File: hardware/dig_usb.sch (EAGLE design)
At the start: 123 parts, among them IC201 ATMEGA32A-AU, IC202 DS1337S, IC203 MAX487CSA, IC204 74HC166D, IC205 74HC595D, IC301 LTV-356T, IC302 LTV-356T, IC303 LTV-356T, IC304 LTV-356T, IC305 LTV-356T, IC306 LTV-356T, IC307 LTV-356T, IC308 LTV-356T, K401 S202S02, K402 S202S02, K403 S202S02, K404 S202S02, K405 S202S02, K406 S202S02, K407 S202S02, K408 S202S02, Q201 32,768kHz, T301 BCR191, T302 BCR191, T303 BCR191, T304 BCR191, T305 BCR191, T306 BCR191, T307 BCR191, T308 BCR191, X101 RIA-73-02, X201 ISP, X202 RIA-73-02, X301 RIA-73-02, X302 RIA-73-02, X303 RIA-73-02, X304 RIA-73-02, X305 RIA-73-02, X401 RIA-73-02, X402 RIA-73-02, X403 RIA-73-02, X404 RIA-73-02, X405 RIA-73-02

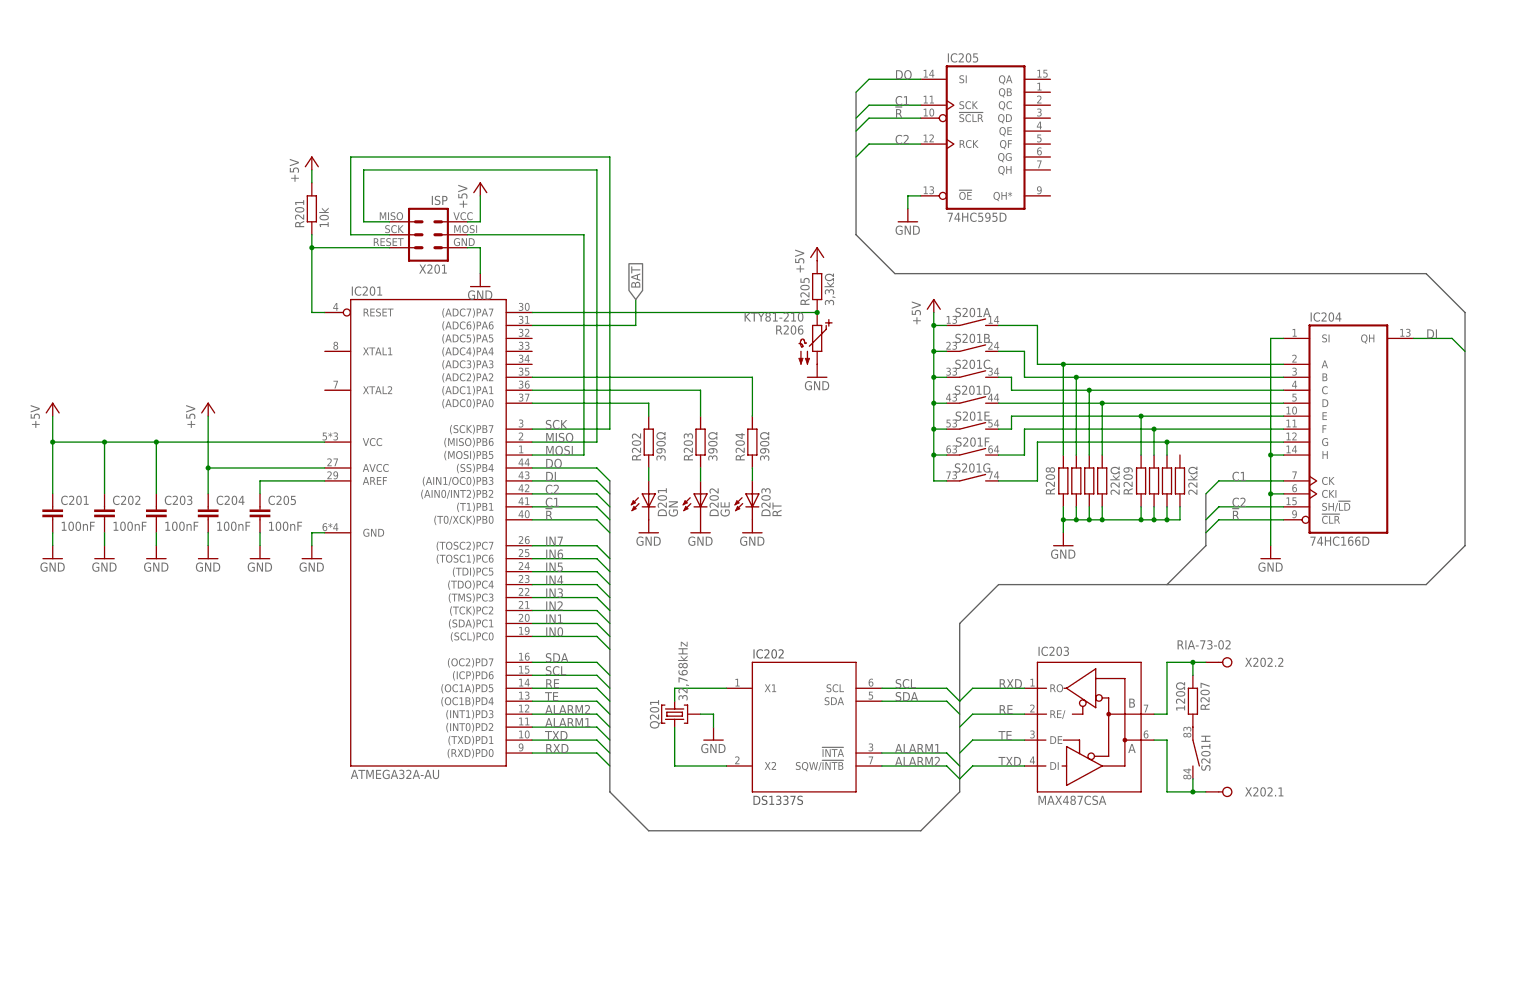
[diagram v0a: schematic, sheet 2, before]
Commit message: dig_usb auf AT90USB1287 umgestellt
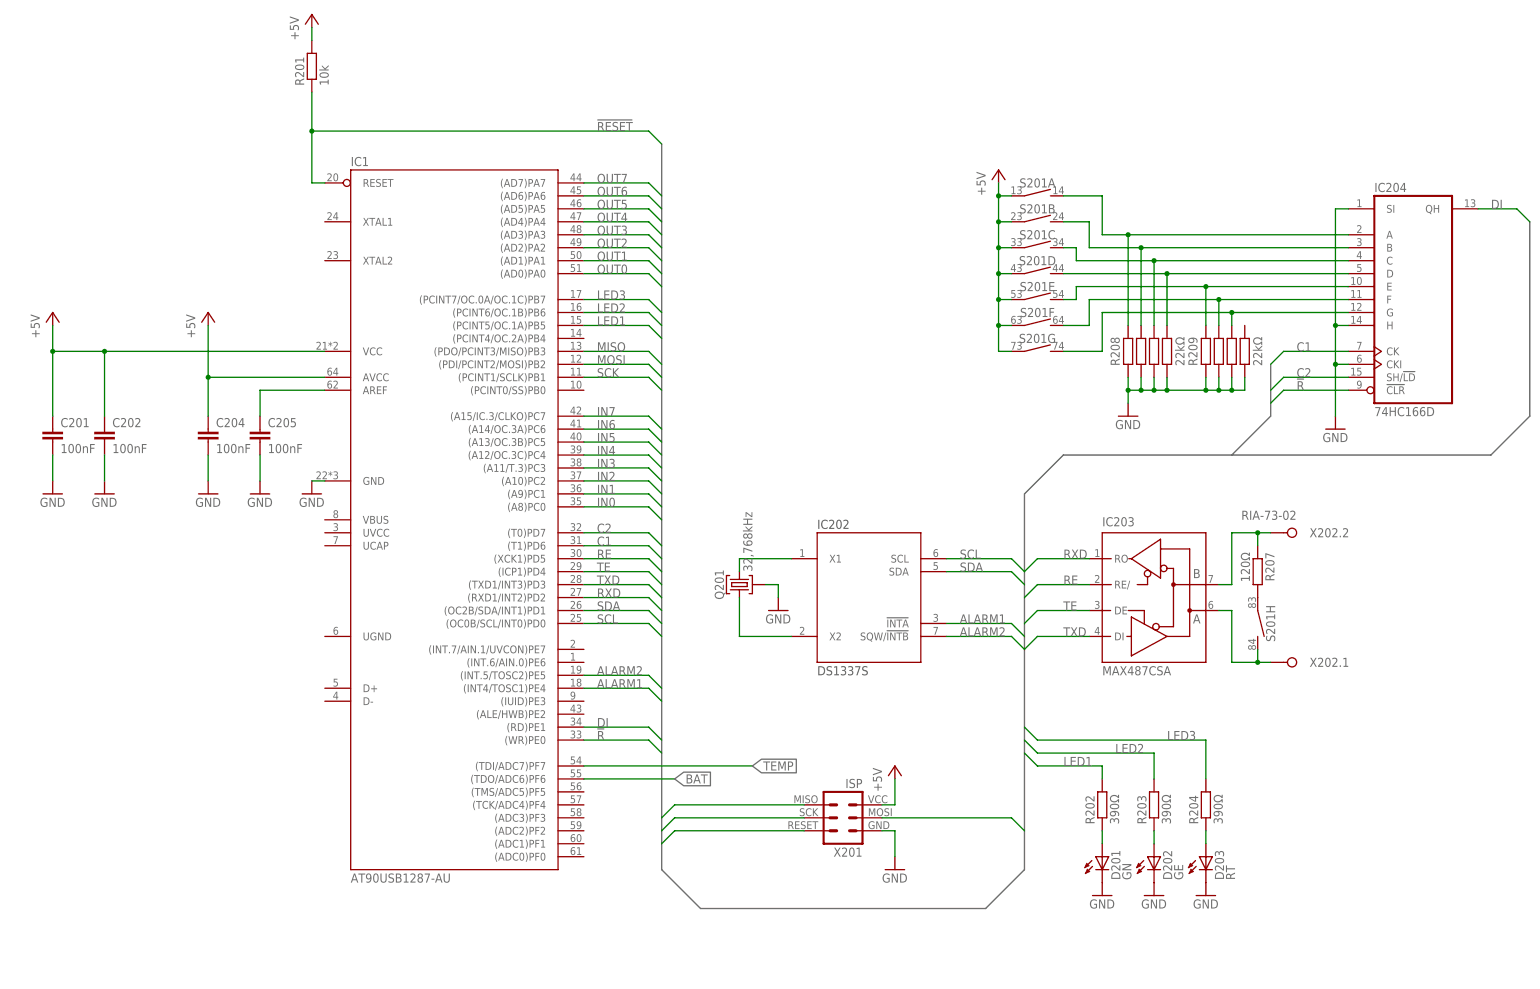
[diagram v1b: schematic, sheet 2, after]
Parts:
- removed C103, C203: 100nF, passiv:C_0603
- removed IC201: ATMEGA32A-AU, ic-mcu:ATMEGA32A-AU
- removed IC205: 74HC595D, ic-logik:74HC595D
- added IC1: AT90USB1287-AU, ic-mcu:AT90USB1287-AU
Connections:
- removed net DO: IC201.(SS)PB4, IC205A.SI
- removed net N$25: C205.1, IC201.AREF
- removed net N$42: IC201.RESET, R201.1, X201.RESET
- removed net N$61: IC201.(ADC7)PA7, R205.1, R206.1
- removed net N$8: IC201.(ADC2)PA2, R204.2
- removed net N$90: IC201.(ADC0)PA0, R202.2
- removed net N$92: IC201.(ADC1)PA1, R203.2
- new net !RESET: IC1.RESET, R201.1, X201.RESET
- new net LED1: IC1.(PCINT5/OC.1A)PB5, R202.2
- new net LED2: IC1.(PCINT6/OC.1B)PB6, R203.2
- new net LED3: IC1.(PCINT7/OC.0A/OC.1C)PB7, R204.2
- new net N$12: C205.1, IC1.AREF
- new net OUT0: IC1.(AD0)PA0
- new net OUT1: IC1.(AD1)PA1
- new net OUT2: IC1.(AD2)PA2
- new net OUT3: IC1.(AD3)PA3
- new net OUT4: IC1.(AD4)PA4
- new net OUT5: IC1.(AD5)PA5
- new net OUT6: IC1.(AD6)PA6
- new net OUT7: IC1.(AD7)PA7
- new net TEMP: IC1.(TDI/ADC7)PF7, R205.1, R206.1
- net !R: now also IC1.(WR)PE0; no longer IC201.(T0/XCK)PB0, IC205A.!SCLR
- net +5V: now also IC1.AVCC, IC1.VCC; no longer C103.1, C203.1, IC201.AVCC, IC201.VCC, IC205P.VCC
- net ALARM1: now also IC1.(INT4/TOSC1)PE4; no longer IC201.(INT0)PD2
- net ALARM2: now also IC1.(INT.5/TOSC2)PE5; no longer IC201.(INT1)PD3
- net BAT: now also IC1.(TDO/ADC6)PF6; no longer IC201.(ADC6)PA6
- net C1: now also IC1.(T1)PD6; no longer IC201.(T1)PB1, IC205A.SCK
- net C2: now also IC1.(T0)PD7; no longer IC201.(AIN0/INT2)PB2, IC205A.RCK
- net DI: now also IC1.(RD)PE1; no longer IC201.(AIN1/OC0)PB3
- net GND: now also IC1.GND; no longer C103.2, C203.2, IC201.GND, IC205A.!OE, IC205P.GND
- net IN0: now also IC1.(A8)PC0; no longer IC201.(SCL)PC0
- net IN1: now also IC1.(A9)PC1; no longer IC201.(SDA)PC1
- net IN2: now also IC1.(A10)PC2; no longer IC201.(TCK)PC2
- net IN3: now also IC1.(A11/T.3)PC3; no longer IC201.(TMS)PC3
- net IN4: now also IC1.(A12/OC.3C)PC4; no longer IC201.(TDO)PC4
- net IN5: now also IC1.(A13/OC.3B)PC5; no longer IC201.(TDI)PC5
- net IN6: now also IC1.(A14/OC.3A)PC6; no longer IC201.(TOSC1)PC6
- net IN7: now also IC1.(A15/IC.3/CLKO)PC7; no longer IC201.(TOSC2)PC7
- net MISO: now also IC1.(PDO/PCINT3/MISO)PB3; no longer IC201.(MISO)PB6
- net MOSI: now also IC1.(PDI/PCINT2/MOSI)PB2; no longer IC201.(MOSI)PB5
- net RE: now also IC1.(XCK1)PD5; no longer IC201.(OC1A)PD5
- net RXD: now also IC1.(RXD1/INT2)PD2; no longer IC201.(RXD)PD0
- net SCK: now also IC1.(PCINT1/SCLK)PB1; no longer IC201.(SCK)PB7
- net SCL: now also IC1.(OC0B/SCL/INT0)PD0; no longer IC201.(ICP)PD6
- net SDA: now also IC1.(OC2B/SDA/INT1)PD1; no longer IC201.(OC2)PD7
- net TE: now also IC1.(ICP1)PD4; no longer IC201.(OC1B)PD4
- net TXD: now also IC1.(TXD1/INT3)PD3; no longer IC201.(TXD)PD1
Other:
- moved on the sheet: C104, C201, C202, C204, C205, D103, D104, D201, D202, D203, G102, IC202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

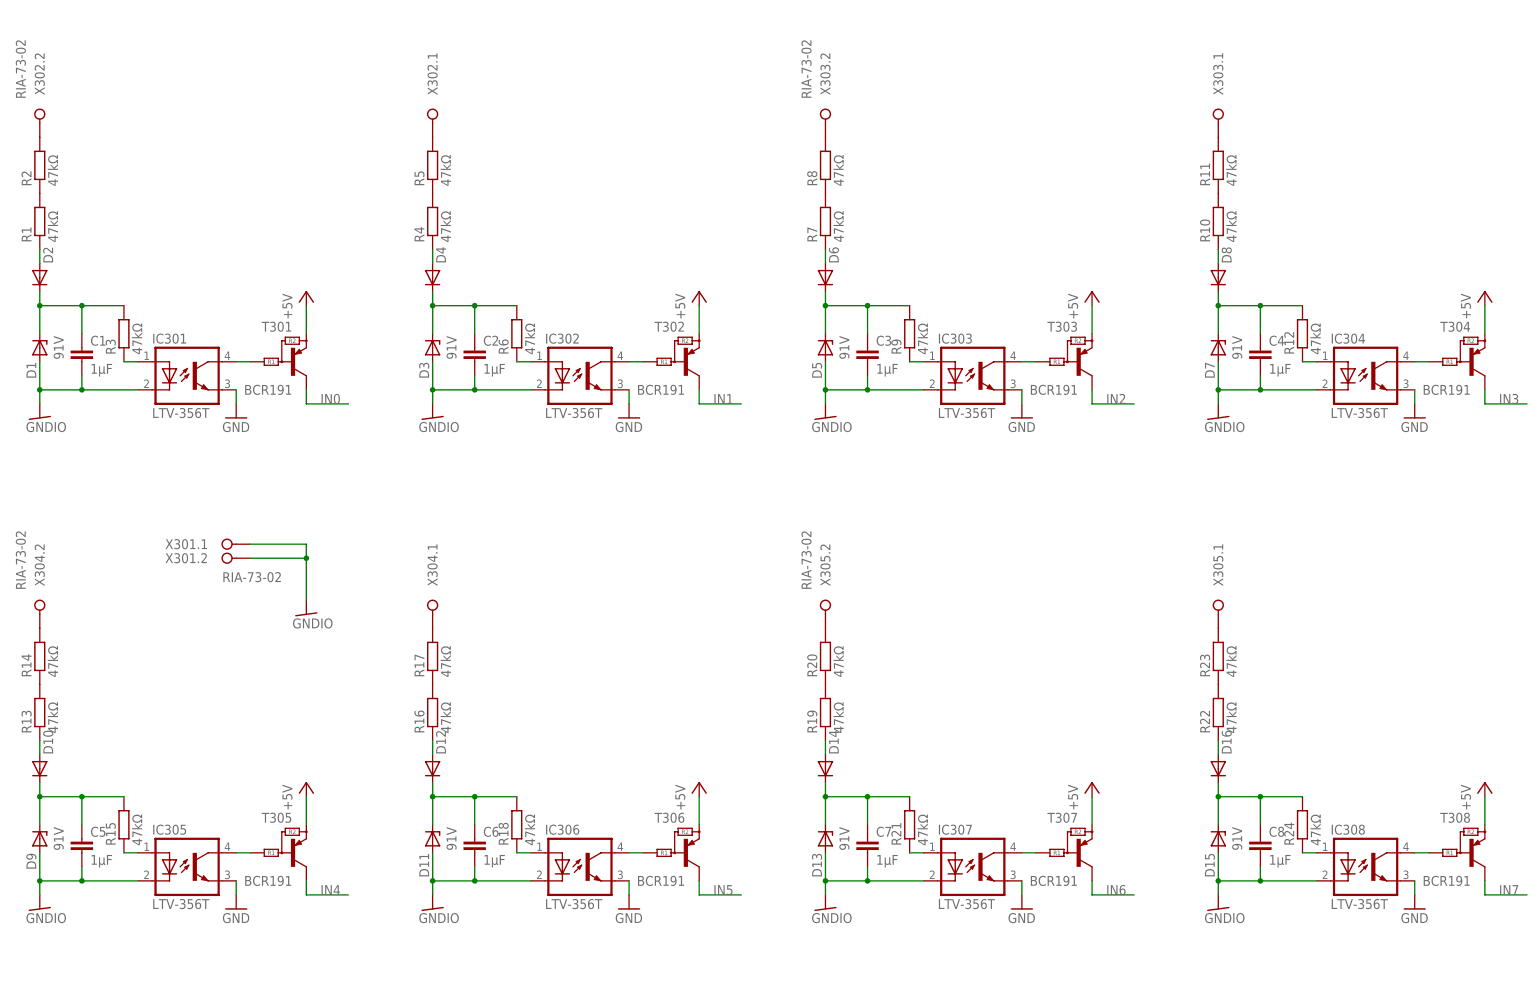
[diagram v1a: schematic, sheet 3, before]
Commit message: IO Bereich der unteren Platine geroutet
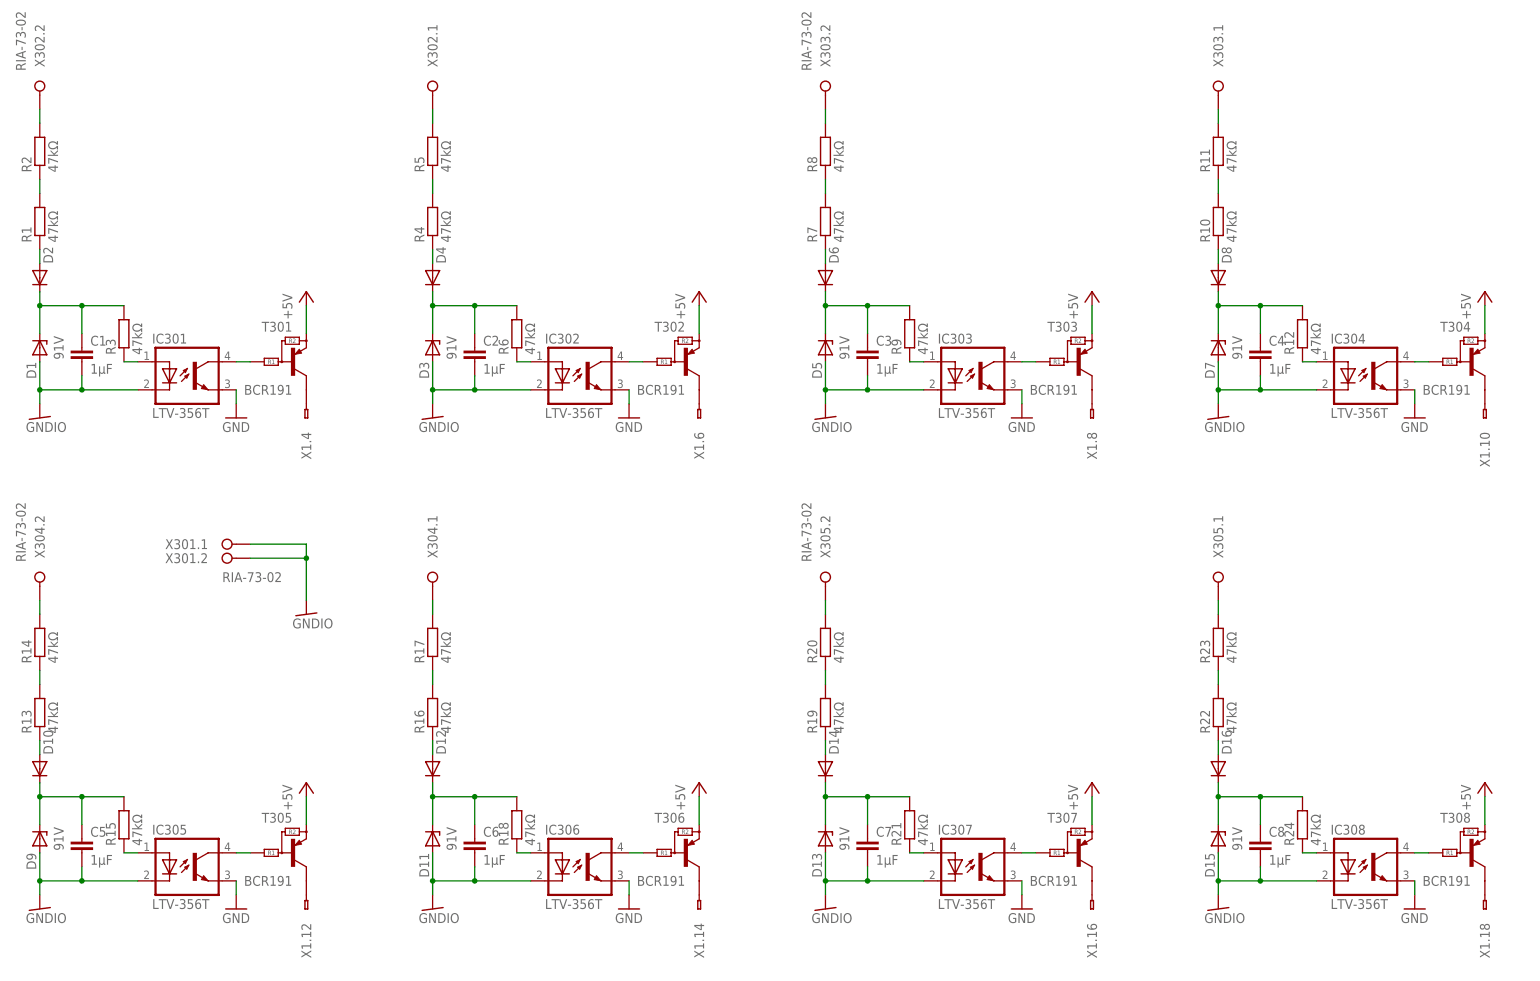
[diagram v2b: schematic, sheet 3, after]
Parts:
- removed R205: 3,3kΩ, passiv:R_0805
- removed R206: KTY81-210, sensor:KTY81-210
- added R401, R402, R403, R404, R405, R406, R407, R408: (no value), passiv:R_0805
- added R409: 3,3kΩ, passiv:R_0805
- added R410: KTY81-210, sensor:KTY81-210
- added X1: (no value), anschluss:WS20V
- G102: value KZH20P -> KZH20SMD-2; device batterie:KZH20P -> batterie:KZH20SMD-2
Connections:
- new net N$100: T307.C, X1.16.A
- new net N$101: T308.C, X1.18.A
- new net N$16: K402.A, R402.2
- new net N$25: K403.A, R403.2
- new net N$37: K404.A, R404.2
- new net N$42: K405.A, R405.2
- new net N$50: K406.A, R406.2
- new net N$61: K407.A, R407.2
- new net N$66: K408.A, R408.2
- new net N$67: R401.1, X1.3.A
- new net N$79: R402.1, X1.5.A
- new net N$8: K401.A, R401.2
- new net N$87: R403.1, X1.7.A
- new net N$88: R404.1, X1.9.A
- new net N$90: R405.1, X1.11.A
- new net N$91: R406.1, X1.13.A
- new net N$92: R407.1, X1.15.A
- new net N$93: R408.1, X1.17.A
- new net N$94: T301.C, X1.4.A
- new net N$95: T302.C, X1.6.A
- new net N$96: T303.C, X1.8.A
- new net N$97: T304.C, X1.10.A
- new net N$98: T305.C, X1.12.A
- new net N$99: T306.C, X1.14.A
- net +5V: now also R409.2, X1.1.A, X1.20.A; no longer R205.2
- net GND: now also R410.2, X1.19.A, X1.2.A; no longer R206.2
- net IN0: no longer T301.C
- net IN1: no longer T302.C
- net IN2: no longer T303.C
- net IN3: no longer T304.C
- net IN4: no longer T305.C
- net IN5: no longer T306.C
- net IN6: no longer T307.C
- net IN7: no longer T308.C
- net TEMP: now also R409.1, R410.1; no longer R205.1, R206.1
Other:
- moved on the sheet: R11, R14, R17, R2, R20, R23, R5, R8, X302.1, X302.2, X303.1, X303.2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

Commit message: Einiges auf dig_usb controllerboard gerouted
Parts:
- removed R101, R202, R203, R204: 390Ω, passiv:R_0805
- added D17, D18, D19, D20, D21, D22, D23, D24, D25, D26, D27, D28, D29, D30, D31, D32: GN, led:LED_0805
- added R25, R26, R27, R28, R29: 1,5kΩ, widerstandsnetzwerk:EXB-38V
- added X2: (no value), anschluss:WS20V
- R401, R402, R403, R404, R405, R406, R407, R408: value (none) -> 470Ω
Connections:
- new net N$102: D17.A, R25.2
- new net N$103: D18.A, R25.4
- new net N$104: D19.A, R25.6
- new net N$105: D20.A, R25.8
- new net N$106: D21.A, R26.2
- new net N$107: D22.A, R26.4
- new net N$108: D23.A, R26.6
- new net N$109: D24.A, R26.8
- new net N$110: D25.A, R27.1
- new net N$111: D26.A, R27.3
- new net N$112: D27.A, R27.5
- new net N$113: D28.A, R27.7
- new net N$114: D29.A, R28.1
- new net N$115: D30.A, R28.3
- new net N$116: D31.A, R28.5
- new net N$117: D32.A, R28.7
- net +5V: now also R29.8, X2.1.A, X2.20.A; no longer R101.2
- net GND: now also D17.C, D18.C, D19.C, D20.C, D21.C, D22.C, D23.C, D24.C, D25.C, D26.C, D27.C, D28.C, D29.C, D30.C, D31.C, D32.C, X2.19.A, X2.2.A
- net IN0: now also R25.1, X2.4.A
- net IN1: now also R25.3, X2.6.A
- net IN2: now also R25.5, X2.8.A
- net IN3: now also R25.7, X2.10.A
- net IN4: now also R26.1, X2.12.A
- net IN5: now also R26.3, X2.14.A
- net IN6: now also R26.5, X2.16.A
- net IN7: now also R26.7, X2.18.A
- net LED1: now also R29.2; no longer R202.2
- net LED2: now also R29.4; no longer R203.2
- net LED3: now also R29.6; no longer R204.2
- net N$4: now also R29.5; no longer R204.1
- net N$44: now also R29.7; no longer R101.1
- net N$62: now also R29.1; no longer R202.1
- net N$63: now also R29.3; no longer R203.1
- net OUT0: now also R27.2, X2.3.A
- net OUT1: now also R27.4, X2.5.A
- net OUT2: now also R27.6, X2.7.A
- net OUT3: now also R27.8, X2.9.A
- net OUT4: now also R28.2, X2.11.A
- net OUT5: now also R28.4, X2.13.A
- net OUT6: now also R28.6, X2.15.A
- net OUT7: now also R28.8, X2.17.A
